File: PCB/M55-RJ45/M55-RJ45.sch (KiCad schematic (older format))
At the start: 2 parts

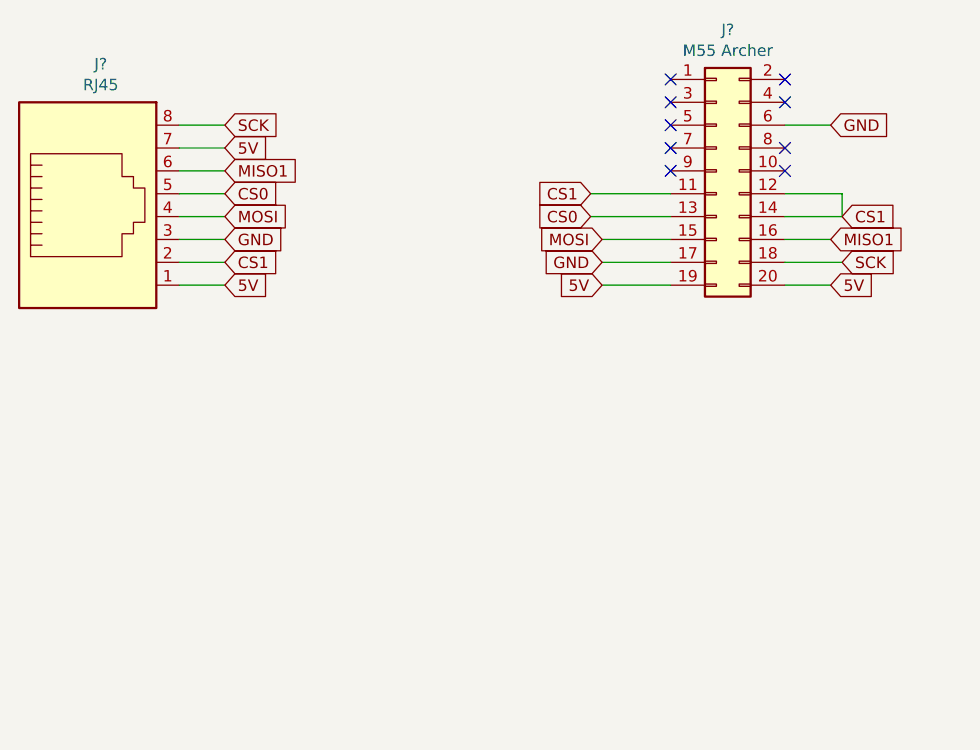
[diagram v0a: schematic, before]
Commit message: two sided layout
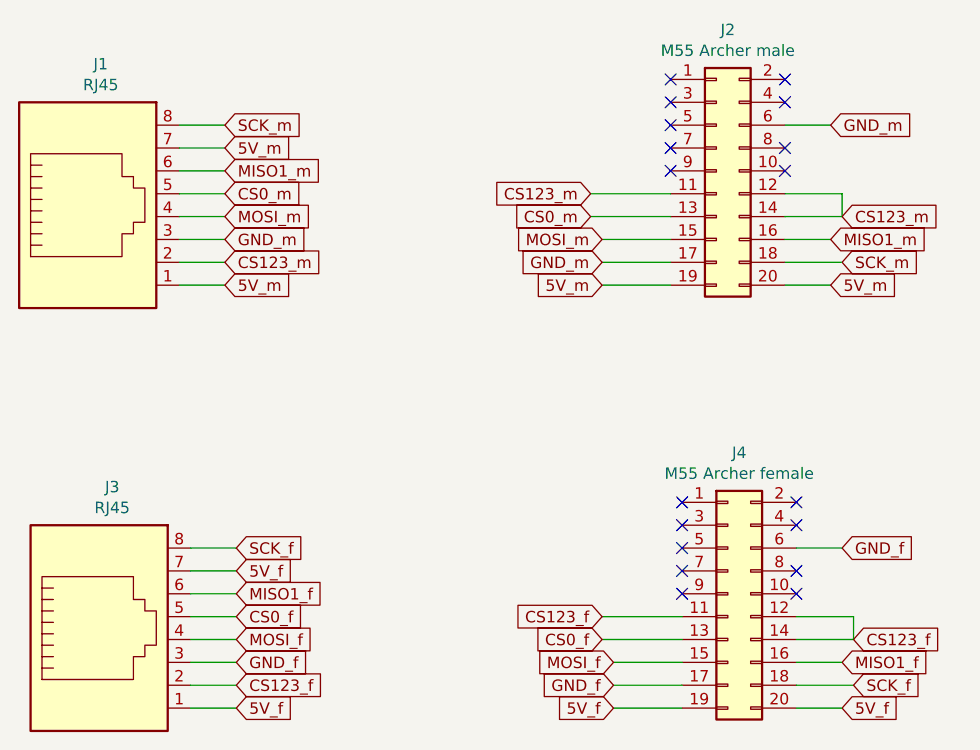
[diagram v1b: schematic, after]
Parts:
- added J3: RJ45, connectors:RJ45_Molex_0855135013_Vertical, symbol Connector:RJ45
- added J4: M55 Archer female, connectors:M55-6XX2042R_Archer_Kontrol, symbol Connector_Generic:Conn_02x10_Odd_Even
- J2: renamed from J?; value M55 Archer -> M55 Archer male; footprint connectors:M55-6XX2042R_Archer_Kontrol -> connectors:M55-7XX2042R_Archer_Kontrol
- gave numbers to parts that had none: 1
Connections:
- net 5V renamed 5V_m
- net CS0 renamed CS0_m
- net CS1 renamed CS123_m
- net GND renamed GND_m
- net MISO1 renamed MISO1_m
- net MOSI renamed MOSI_m
- net SCK renamed SCK_m
- new net 5V_f: J3.1, J3.7, J4.19 (Pin_19), J4.20 (Pin_20)
- new net CS0_f: J3.5, J4.13 (Pin_13)
- new net CS123_f: J3.2, J4.11 (Pin_11), J4.12 (Pin_12), J4.14 (Pin_14)
- new net GND_f: J3.3, J4.17 (Pin_17), J4.6 (Pin_6)
- new net MISO1_f: J3.6, J4.16 (Pin_16)
- new net MOSI_f: J3.4, J4.15 (Pin_15)
- new net SCK_f: J3.8, J4.18 (Pin_18)
- no-connect marks 9 -> 18
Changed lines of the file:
@@
 $EndDescr
 $Comp
-L Connector:RJ45 J?
+L Connector:RJ45 J1
 U 1 1 5E7232B4
 P 2400 2350
-F 0 "J?" H 2457 3017 50  0000 C CNN
+F 0 "J1" H 2457 3017 50  0000 C CNN
 F 1 "RJ45" H 2457 2926 50  0000 C CNN
 F 2 "connectors:RJ45_Molex_0855135013_Vertical" V 2400 2375 50  0001 C CNN
@@
 $EndComp
 $Comp
-L Connector_Generic:Conn_02x10_Odd_Even J?
+L Connector_Generic:Conn_02x10_Odd_Even J2
 U 1 1 5E724F0C
 P 5150 2150
-F 0 "J?" H 5200 2767 50  0000 C CNN
-F 1 "M55 Archer" H 5200 2676 50  0000 C CNN
-F 2 "connectors:M55-6XX2042R_Archer_Kontrol" H 5150 2150 50  0001 C CNN
+F 0 "J2" H 5200 2767 50  0000 C CNN
+F 1 "M55 Archer male" H 5200 2676 50  0000 C CNN
+F 2 "connectors:M55-7XX2042R_Archer_Kontrol" H 5150 2150 50  0001 C CNN
 F 3 "~" H 5150 2150 50  0001 C CNN
 	1    5150 2150
@@
 NoConn ~ 5450 2150
 Text GLabel 5700 2550 2    50   Input ~ 0
-SCK
+SCK_m
 Text GLabel 4650 2450 0    50   Input ~ 0
-MOSI
+MOSI_m
 Text GLabel 5650 2450 2    50   Input ~ 0
-MISO1
+MISO1_m
 Text GLabel 4600 2350 0    50   Input ~ 0
-CS0
+CS0_m
 Text GLabel 5700 2350 2    50   Input ~ 0
-CS1
+CS123_m
 Wire Wire Line
 	5450 2550 5700 2550
@@
 	5450 2350 5700 2350
 Text GLabel 3000 2150 2    50   Input ~ 0
-MISO1
+MISO1_m
 Text GLabel 3000 2250 2    50   Input ~ 0
-CS0
+CS0_m
 Text GLabel 3000 2550 2    50   Input ~ 0
-CS1
+CS123_m
 Text GLabel 3000 2350 2    50   Input ~ 0
-MOSI
+MOSI_m
 Text GLabel 3000 1950 2    50   Input ~ 0
-SCK
+SCK_m
 Wire Wire Line
 	3000 1950 2800 1950
@@
 	3000 2350 2800 2350
 Text GLabel 4600 2250 0    50   Input ~ 0
-CS1
+CS123_m
 Wire Wire Line
 	4950 2250 4600 2250
@@
 	3000 2150 2800 2150
 Text GLabel 3000 2450 2    50   Input ~ 0
-GND
+GND_m
 Text GLabel 3000 2650 2    50   Input ~ 0
-5V
+5V_m
 Wire Wire Line
 	3000 2450 2800 2450
 Text GLabel 3000 2050 2    50   Input ~ 0
-5V
+5V_m
 Wire Wire Line
 	3000 2050 2800 2050
@@
 	2800 2650 3000 2650
 Text GLabel 5650 1950 2    50   Input ~ 0
-GND
+GND_m
 Text GLabel 4650 2550 0    50   Input ~ 0
-GND
+GND_m
 Wire Wire Line
 	4650 2550 4950 2550
 Text GLabel 4650 2650 0    50   Input ~ 0
-5V
+5V_m
 Wire Wire Line
 	4650 2650 4950 2650
 Text GLabel 5650 2650 2    50   Input ~ 0
-5V
+5V_m
 Wire Wire Line
 	5650 2650 5450 2650
 Wire Wire Line
 	5650 1950 5450 1950
+$Comp
+L Connector:RJ45 J3
+U 1 1 5E745911
+P 2450 4200
+F 0 "J3" H 2507 4867 50  0000 C CNN
+F 1 "RJ45" H 2507 4776 50  0000 C CNN
+F 2 "connectors:RJ45_Molex_0855135013_Vertical" V 2450 4225 50  0001 C CNN
+F 3 "~" V 2450 4225 50  0001 C CNN
+	1    2450 4200
+	1    0    0    -1
+$EndComp
+$Comp
+L Connector_Generic:Conn_02x10_Odd_Even J4
+U 1 1 5E745917
+P 5200 4000
+F 0 "J4" H 5250 4617 50  0000 C CNN
+F 1 "M55 Archer female" H 5250 4526 50  0000 C CNN
+F 2 "connectors:M55-6XX2042R_Archer_Kontrol" H 5200 4000 50  0001 C CNN
+F 3 "~" H 5200 4000 50  0001 C CNN
+	1    5200 4000
+	1    0    0    -1
+$EndComp
+NoConn ~ 5000 3600
+NoConn ~ 5500 3600
+NoConn ~ 5000 3700
+NoConn ~ 5500 3700
+NoConn ~ 5000 3800
+NoConn ~ 5000 3900
+NoConn ~ 5500 3900
+NoConn ~ 5000 4000
+NoConn ~ 5500 4000
+Text GLabel 5750 4400 2    50   Input ~ 0
+SCK_f
+Text GLabel 4700 4300 0    50   Input ~ 0
+MOSI_f
+Text GLabel 5700 4300 2    50   Input ~ 0
+MISO1_f
+Text GLabel 4650 4200 0    50   Input ~ 0
+CS0_f
+Text GLabel 5750 4200 2    50   Input ~ 0
+CS123_f
+Wire Wire Line
+	5500 4400 5750 4400
+Wire Wire Line
+	4700 4300 5000 4300
+Wire Wire Line
+	5500 4300 5700 4300
+Wire Wire Line
+	4650 4200 5000 4200
+Wire Wire Line
+	5500 4200 5750 4200
+Text GLabel 3050 4000 2    50   Input ~ 0
+MISO1_f
+Text GLabel 3050 4100 2    50   Input ~ 0
+CS0_f
+Text GLabel 3050 4400 2    50   Input ~ 0
+CS123_f
+Text GLabel 3050 4200 2    50   Input ~ 0
+MOSI_f
+Text GLabel 3050 3800 2    50   Input ~ 0
+SCK_f
+Wire Wire Line
+	3050 3800 2850 3800
+Wire Wire Line
+	3050 4200 2850 4200
+Text GLabel 4650 4100 0    50   Input ~ 0
+CS123_f
+Wire Wire Line
+	5000 4100 4650 4100
+Wire Wire Line
+	5500 4100 5750 4100
+Wire Wire Line
+	5750 4100 5750 4200
+Wire Wire Line
+	3050 4400 2850 4400
+Wire Wire Line
+	3050 4100 2850 4100
+Wire Wire Line
+	3050 4000 2850 4000
+Text GLabel 3050 4300 2    50   Input ~ 0
+GND_f
+Text GLabel 3050 4500 2    50   Input ~ 0
+5V_f
+Wire Wire Line
+	3050 4300 2850 4300
+Text GLabel 3050 3900 2    50   Input ~ 0
+5V_f
+Wire Wire Line
+	3050 3900 2850 3900
+Wire Wire Line
+	2850 4500 3050 4500
+Text GLabel 5700 3800 2    50   Input ~ 0
+GND_f
+Text GLabel 4700 4400 0    50   Input ~ 0
+GND_f
+Wire Wire Line
+	4700 4400 5000 4400
+Text GLabel 4700 4500 0    50   Input ~ 0
+5V_f
+Wire Wire Line
+	4700 4500 5000 4500
+Text GLabel 5700 4500 2    50   Input ~ 0
+5V_f
+Wire Wire Line
+	5700 4500 5500 4500
+Wire Wire Line
+	5700 3800 5500 3800
 $EndSCHEMATC
